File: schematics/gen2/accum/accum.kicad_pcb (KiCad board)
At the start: 2 copper layers, 100 x 91.1 mm, 15 parts, among them U1 74LS574, U2 74LS138, U3 74LS02, U4 74LS245, U5 74LS245, U6 74LS245

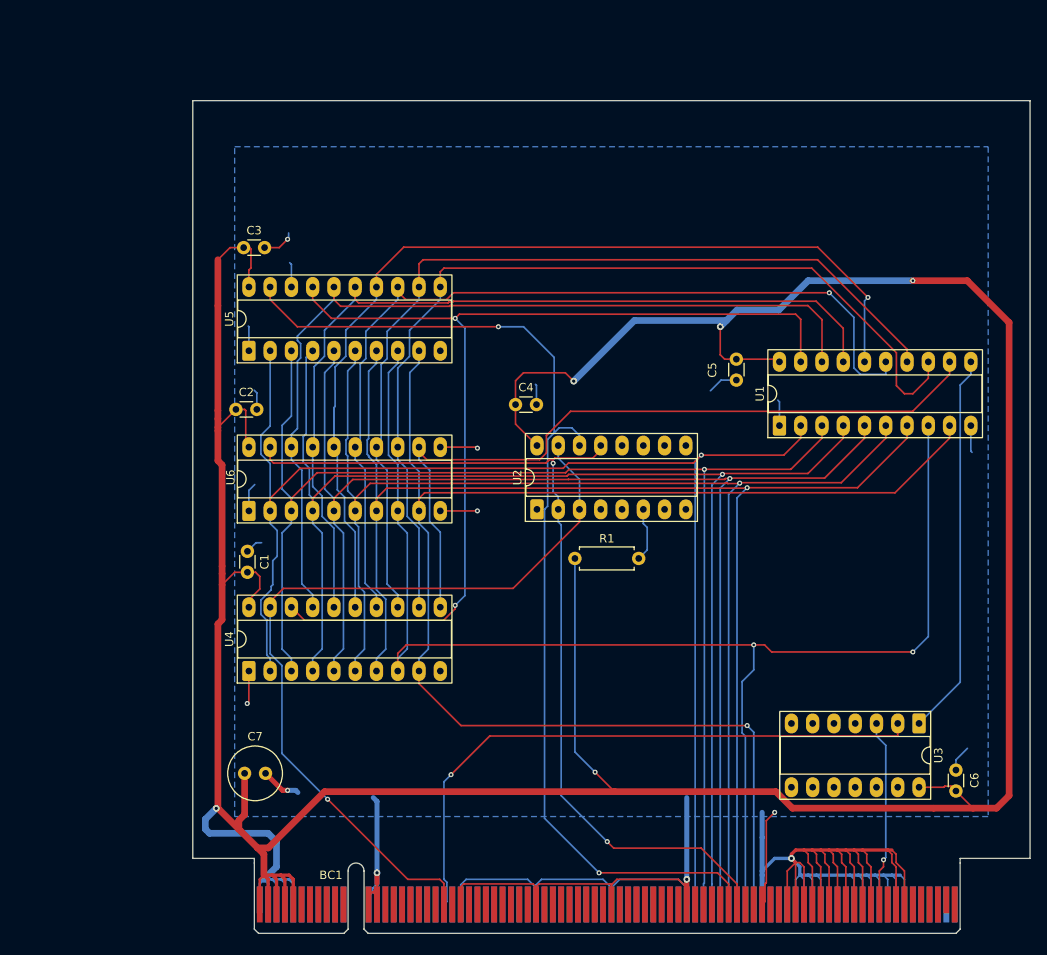
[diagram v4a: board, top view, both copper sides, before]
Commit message: refactor(accum): reimplemented accumalot module
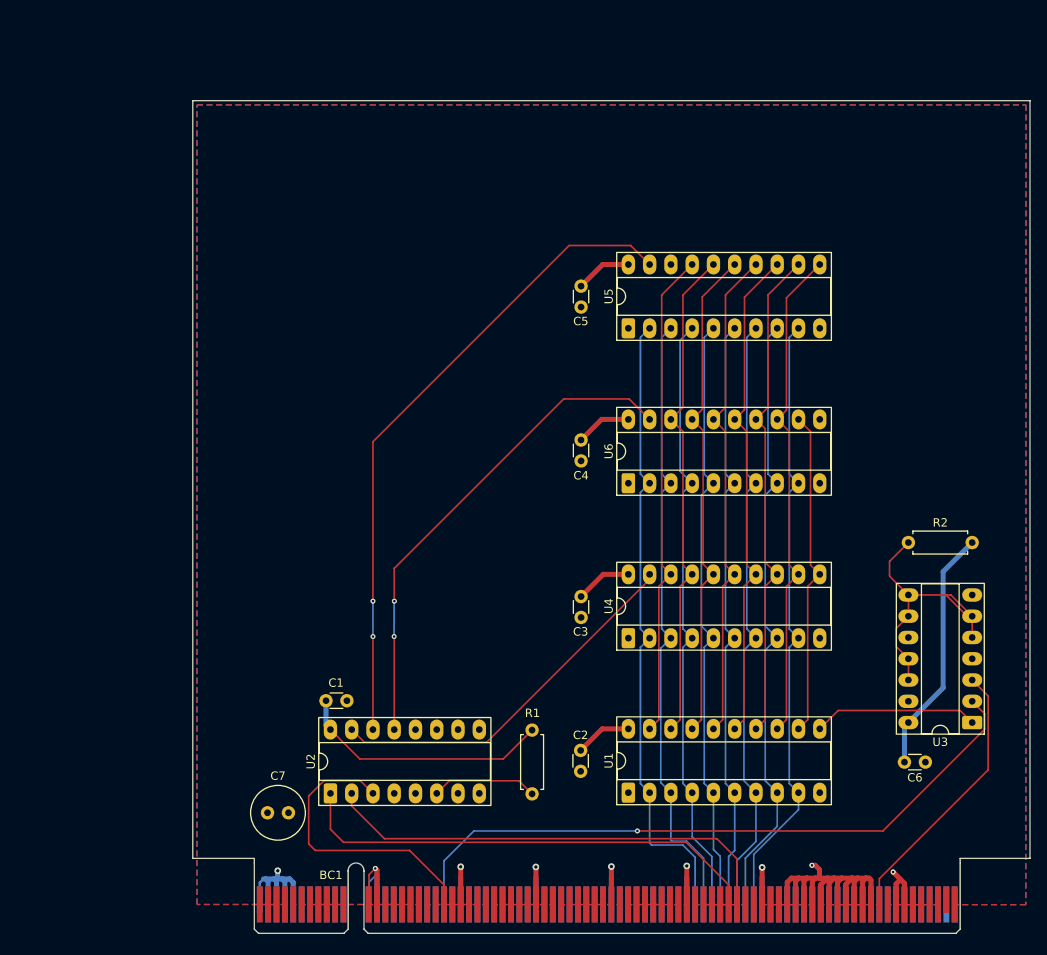
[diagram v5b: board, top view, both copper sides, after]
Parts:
- added R2: R, Resistor_THT:R_Axial_DIN0207_L6.3mm_D2.5mm_P7.62mm_Horizontal, F.Cu at (185.5, 102.3)
- moved C3 58.0 mm to (146.4, 108.7), turned to -90 degrees
- moved C2 57.9 mm to (146.3, 127.1), turned to -90 degrees
- moved U1 47.4 mm to (152.0, 132.2)
- moved U4 45.5 mm to (152.0, 113.7)
- moved U6 45.4 mm to (152.0, 95.2)
- moved U5 45.4 mm to (152.0, 76.7)
- moved U2 41.9 mm to (116.4, 132.2)
- moved R1 21.1 mm to (140.5, 124.7), turned to -90 degrees
- moved C5 20.5 mm to (146.4, 71.7)
- moved C1 18.0 mm to (115.9, 121.2), turned to 0 degrees
- moved C4 8.89 mm to (146.4, 90.0), turned to -90 degrees
- moved C6 7.05 mm to (185.0, 128.5), turned to 0 degrees
- moved U3 6.35 mm to (193.1, 123.8), turned to 180 degrees
- moved C7 5.45 mm to (108.9, 134.6)
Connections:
- BC1 pad B21: /~{RAC} -> /~{PASS}
- BC1 pad B55: /ACSHLEFT -> /SHL
- BC1 pad B56: /ACSHRIGHT -> /SHR
- U2 pad 1: /ACSHLEFT -> /SHL
- U2 pad 2: /ACSHRIGHT -> /SHR
- U2 pad 3: /~{RAC} -> /~{PASS}
- U3 pad 11: unconnected-(U3-Pad11) -> Net-(R2-Pad1)
- U3 pad 12: unconnected-(U3-Pad12) -> Net-(R2-Pad1)
- U3 pad 5: unconnected-(U3-Pad5) -> Net-(R2-Pad1)
- U3 pad 6: unconnected-(U3-Pad6) -> Net-(R2-Pad1)
- U3 pad 8: unconnected-(U3-Pad8) -> Net-(R2-Pad1)
- U3 pad 9: unconnected-(U3-Pad9) -> Net-(R2-Pad1)
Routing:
- net VCC: track 444.7 -> 107.5 mm, vias 5 -> 1
- net GND: track 342.1 -> 111.2 mm, vias 9 -> 8
- net /DATA7: track 173.9 -> 73.8 mm, vias 1 -> 0
- net /DATA6: track 164.0 -> 73.7 mm, vias 2 -> 0
- net /DATA3: track 160.8 -> 72.2 mm, vias 1 -> 0
- net /DATA2: track 161.4 -> 72.8 mm, vias 1 -> 0
- net /DATA4: track 160.4 -> 71.9 mm, vias 1 -> 0
- net /DATA0: track 164.1 -> 76.0 mm, vias 1 -> 0
- net /DATA1: track 161.4 -> 74.3 mm, vias 1 -> 0
- net /DATA5: track 159.7 -> 72.8 mm, vias 1 -> 0
- net /ACCUM0: track 122.7 -> 58.5 mm, vias 2 -> 0
- net /ACCUM3: track 118.0 -> 59.7 mm, vias 1 -> 0
- net /SHL: track 0.00 -> 56.9 mm
- net /SHR: track 0.00 -> 55.6 mm
- net /ACCUM6: track 112.9 -> 59.7 mm
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- added copper zone on F.Cu, net VCC

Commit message: update core_2
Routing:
- net /~{CLK}: track 33.0 -> 34.2 mm
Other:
- board text added: "ACCUMULATOR"

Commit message: accum review complete
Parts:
- C1, C2, C3, C4, C5, C6: footprint Capacitor_THT:C_Disc_D3.0mm_W1.6mm_P2.50mm -> Capacitor_THT:C_Disc_D5.0mm_W2.5mm_P5.00mm
- moved C3 2.26 mm to (146.0, 106.5)
- turned C1 to 90 degrees
- turned C6 to 180 degrees
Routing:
- net VCC: track 107.5 -> 114.3 mm

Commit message: accum review complete final
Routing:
- net Net-(R2-Pad1): track 35.3 -> 30.9 mm
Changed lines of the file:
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@@
-	)
-	(segment
-		(start 189.95 108.535)
-		(end 193.09 111.675)
-		(width 0.2)
-		(layer "F.Cu")
-		(net 107)
 	)
 	(segment
